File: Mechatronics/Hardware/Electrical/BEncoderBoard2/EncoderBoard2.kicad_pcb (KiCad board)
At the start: 2 copper layers, 37.8 x 59.2 mm, 66 parts, among them IC1 TP4056, IC2 DW01+G, J1 Conn_01x08_Male, J2 Conn_01x07_Male, J3 Barrel_Jack_Switch, J4 GNDPWR, J5 Conn_01x02_Male, J6 Conn_01x04_Male, Q1 DMosfet, Q2 Q_PMOS_GSD, Q3 Q_PMOS_GSD, U1 STM32G431CBT6, U2 ITR1802, U3 ITR1802, U4 RN4871, U5 82402305, U6 LTC3240, Y1 8Mhz

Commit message: Changes
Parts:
- R1, R2: value 220 -> 560
- S1: value EG1218(+3.3v) -> EG1218_Conn
- U2, U3: value ITR1802 -> ITR1802_Conn; footprint Encoder:OptointerrupterSmall -> Encoder:PinHeader_2x02_P2.54mm_Vertical
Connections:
- IC1 pad 6: Net-(IC1-Pad6) -> (no net)
- IC1 pad 7: Net-(IC1-Pad7) -> (no net)
- IC1 pad 9: Net-(IC1-Pad9) -> (no net)
- IC2 pad 4: Net-(IC2-Pad4) -> (no net)
- Q1 pad 2: Net-(Q1-Pad2) -> (no net)
- Q1 pad 5: Net-(Q1-Pad5) -> (no net)
- U1 pad 1: Net-(U1-Pad1) -> (no net)
- U1 pad 12: Net-(U1-Pad12) -> (no net)
- U1 pad 16: Net-(U1-Pad16) -> (no net)
- U1 pad 17: Net-(U1-Pad17) -> (no net)
- U1 pad 2: Net-(U1-Pad2) -> (no net)
- U1 pad 20: Net-(U1-Pad20) -> (no net)
- U1 pad 22: Net-(U1-Pad22) -> (no net)
- U1 pad 25: Net-(U1-Pad25) -> (no net)
- U1 pad 27: Net-(U1-Pad27) -> (no net)
- U1 pad 29: Net-(U1-Pad29) -> (no net)
- U1 pad 3: Net-(U1-Pad3) -> (no net)
- U1 pad 33: Net-(U1-Pad33) -> (no net)
- U1 pad 34: Net-(U1-Pad34) -> (no net)
- U1 pad 4: Net-(U1-Pad4) -> (no net)
- U1 pad 41: Net-(U1-Pad41) -> (no net)
- U4 pad 1: Net-(U4-Pad1) -> (no net)
- U4 pad 11: Net-(U4-Pad11) -> (no net)
- U4 pad 12: Net-(U4-Pad12) -> (no net)
- U4 pad 15: Net-(U4-Pad15) -> (no net)
- U4 pad 3: Net-(U4-Pad3) -> (no net)
- U4 pad 4: Net-(U4-Pad4) -> (no net)
- U4 pad 5: Net-(U4-Pad5) -> (no net)
- U4 pad 6: Net-(U4-Pad6) -> (no net)
- U4 pad 9: Net-(U4-Pad9) -> (no net)
- U5 pad 1: Net-(U5-Pad1) -> (no net)
- U5 pad 3: Net-(U5-Pad3) -> (no net)
- U5 pad 4: Net-(U5-Pad4) -> (no net)
- U5 pad 6: Net-(U5-Pad6) -> (no net)

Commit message: Changed name
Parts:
- U2, U3: value ITR1802_Conn -> ITR8102_Conn

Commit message: Changed files
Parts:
- U2, U3: value ITR8102_Conn -> OPTO_Conn

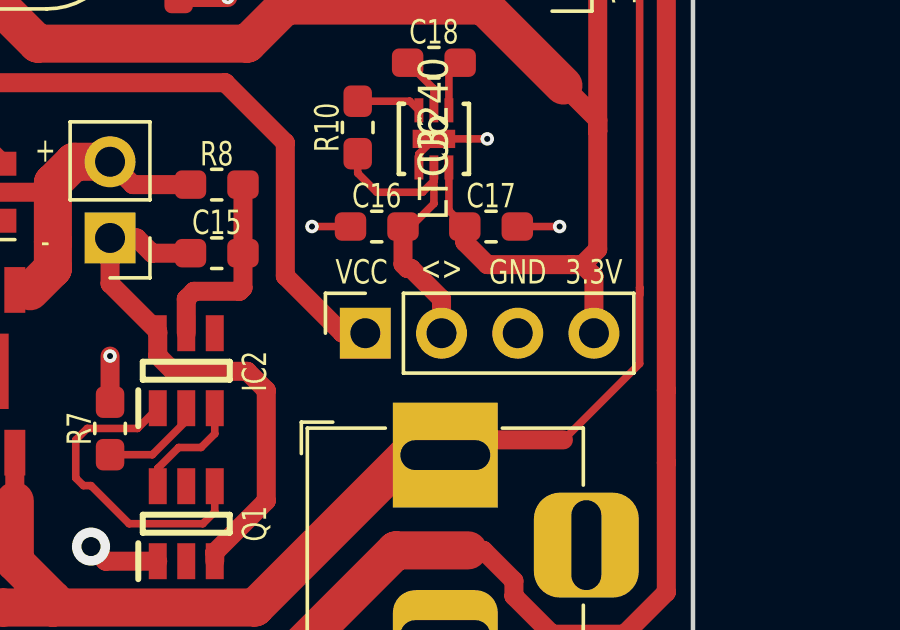
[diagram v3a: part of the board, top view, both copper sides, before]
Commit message: pin header change
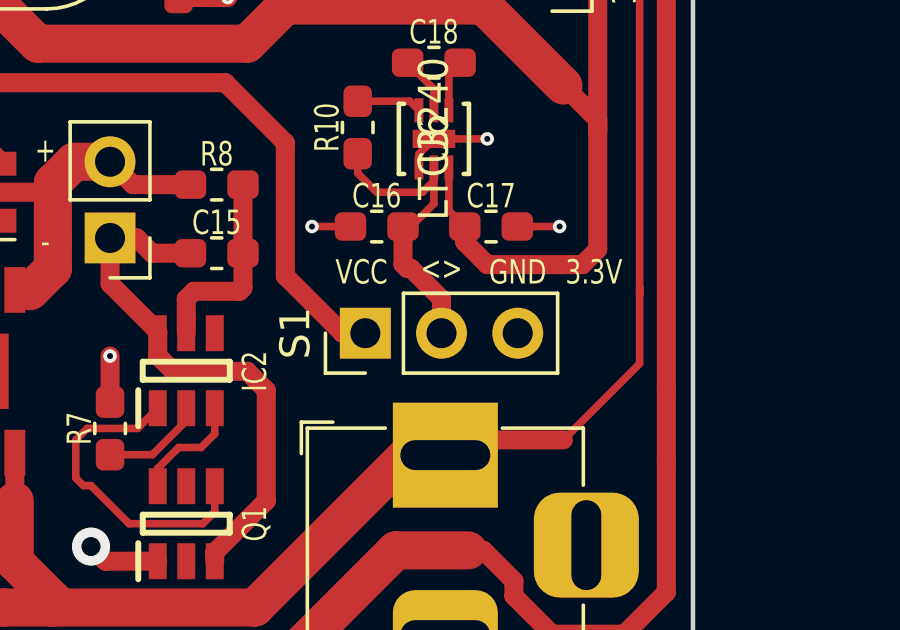
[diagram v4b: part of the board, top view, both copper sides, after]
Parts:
- J1: value Conn_01x08_Male -> MagSensors_Conn
- J2: value Conn_01x07_Male -> OLED/SWD_Conn
- J5: value Conn_01x02_Male -> Batt_Conn
- J6: value Conn_01x04_Male -> MagSensors_Power
- S1: footprint Encoder:PinHeader_1x04_P2.54mm_Vertical -> Encoder:PinHeader_1x03_P2.54mm_Vertical
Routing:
- net +3V3: track 246.3 -> 243.9 mm

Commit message: Changes
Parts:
- R6: value 1.2K -> 1.5K

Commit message: Changes
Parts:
- C15: value .1uF -> 100nF
